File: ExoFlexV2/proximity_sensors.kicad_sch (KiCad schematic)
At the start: 35 parts, among them U31 SN74LVC3G14DCUT_V2, U32 SN74LV4T08PWR_V2, U33 SN74HC7032D_V2, U37 SN74AUP1G17DCKR, U38 SN74AUP1G17DCKR, U39 SN74AUP1G17DCKR, U40 SN74AUP1G17DCKR, U41 SN74AUP1G17DCKR, U8 SN74LV4T08PWR_V2

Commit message: quque truc
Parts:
- removed C92, C93, C94, C95, C96: 0,1uF, Capacitor_SMD:C_0603_1608Metric, symbol Device:C
- removed R47, R48, R49, R50, R51: R_Small_US, Resistor_SMD:R_0603_1608Metric, symbol Device:R_Small_US
- removed TP25, TP27, TP28, TP29: 5005, FootPrint:KEYSTONE_5005, symbol SymLib:5005
- removed U37, U38, U39, U40, U41: SN74AUP1G17DCKR, FootPrint:SN74AUP, symbol SymLib:SN74AUP1G17DCKR
- added R88, R89, R90, R94, R95: 0 ohm, Resistor_SMD:R_0603_1608Metric, symbol Device:R_Small_US
- added TP61, TP62, TP63, TP64, TP65, TP66, TP68, TP69, TP70, TP71, TP72: 5005, FootPrint:KEYSTONE_5005, symbol SymLib:5005
- added U18, U38: 74LV244PW, FootPrint:DB20, symbol SymLib:74LV244PW
- C117: renamed from C87; footprint (none) -> Capacitor_SMD:C_0603_1608Metric
- C118: renamed from C88; footprint (none) -> Capacitor_SMD:C_0603_1608Metric
- C119: renamed from C89; footprint (none) -> Capacitor_SMD:C_0603_1608Metric
- C120: renamed from C90; footprint (none) -> Capacitor_SMD:C_0603_1608Metric
- C121: renamed from C91; footprint (none) -> Capacitor_SMD:C_0603_1608Metric
- renumbered C97 to C122, R42 to R91, R43 to R92, R44 to R93, R45 to R96, R46 to R97, TP26 to TP67, U31 to U33, U32 to U34, U33 to U35, U8 to U9
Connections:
- net +5V: now also U38.20 (VCC)
- net BUT_PROX_1: now also R95.2
- net BUT_PROX_2: now also R94.2
- net BUT_PROX_SEC: now also TP72.TP
- net GND: now also U38.1 (1OE), U38.10 (GND), U38.19 (2OE)
- net PROX_1: now also TP66.TP, U18.5 (2Y1)
- net PROX_2: now also TP67.TP, U18.7 (2Y2)
- net PROX_3: now also TP68.TP, U18.9 (2Y3)
- net PROX_OUT_1: now also R90.2
- net PROX_OUT_2: now also R91.1, R88.2
- net PROX_OUT_3: now also R89.2
- net PROX_SEC: now also TP71.TP
- net at C119.1, R93.2: now also U18.11 (2A3)
- net at C117.1, R91.2: now also U18.13 (2A2)
- net at U9.2 (1B): now also TP70.TP, U38.16 (1Y1)
- net at C120.1, R96.2: now also U38.4 (1A1)
- net at C121.1, R97.2: now also U38.2 (1A0)
- net at C118.1, R92.2: now also U18.15 (2A1)
- net at U9.1 (1A): now also TP69.TP, U38.18 (1Y0)
- new net: R89.1, TP62.TP
- new net: R94.1, TP64.TP
- new net: R90.1, TP63.TP
- new net: R95.1, TP65.TP
- new net: R88.1, TP61.TP
- no-connect marks 5 -> 0
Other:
- moved on the sheet: TP67

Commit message: Placement
Début du placement et modification d'après dernier review
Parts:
- removed R94: 0 ohm, Resistor_SMD:R_0603_1608Metric, symbol Device:R_Small_US
- removed TP64, TP69, TP70: 5005, FootPrint:KEYSTONE_5005, symbol SymLib:5005
- added R84: 0Ω, Resistor_SMD:R_0603_1608Metric, symbol Device:R_Small_US
- added TP107, TP111, TP112, TP113, TP114, TP115: 5005, FootPrint:KEYSTONE_5005, symbol SymLib:5005
- R80: renamed from R90; value 0 ohm -> 0Ω
- R81: renamed from R88; value 0 ohm -> 0Ω
- R82: renamed from R89; value 0 ohm -> 0Ω
- R83: renamed from R95; value 0 ohm -> 0Ω
- renumbered C118 to C121, C117 to C122, C119 to C123, C121 to C124, C120 to C125, C122 to C126, R92 to R85, R91 to R86, R93 to R87, R97 to R88, R96 to R89, TP63 to TP103, TP61 to TP104, TP62 to TP105, TP65 to TP106, TP66 to TP108, TP67 to TP109, TP68 to TP110, TP71 to TP116, TP72 to TP117, U18 to U17, U38 to U18, U9 to U8
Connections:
- net BUT_PROX_2: now also R84.2
- net at U34.11 (4Y), U35.10 (3B): now also TP115.TP
- net at U33.5 (2Y), U34.12 (4A): now also TP113.TP
- net PROX_4: now reaches U18.18 (1Y0), U8.1 (1A)
- net PROX_4: now also TP111.TP
- net PROX_5: now reaches U18.16 (1Y1), U8.2 (1B)
- net PROX_5: now also TP112.TP
- net at U35.6 (2Y), U35.9 (3A): now also TP114.TP
- new net: R84.1, TP107.TP
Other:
- moved on the sheet: C121, C122, C123, C124, C125, R80, R83, R85, R86, R87, R88, R89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

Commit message: Placement encore
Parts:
- removed U17, U18: 74LV244PW, FootPrint:DB20, symbol SymLib:74LV244PW
- added U3: 74LV244PW, FootPrint:DB20, symbol SymLib:74LV244PW
- C122: renamed from C121; value 10 uF -> 10uF
- C123: renamed from C122; value 10 uF -> 10uF
- C124: renamed from C123; value 10 uF -> 10uF
- C125: renamed from C124; value 10 uF -> 10uF
- C126: renamed from C125; value 10 uF -> 10uF
- renumbered C126 to C127, R80 to R81, R81 to R82, R82 to R83, R83 to R84, R84 to R85, R85 to R86, R86 to R87, R87 to R88, R88 to R89, R89 to R90, U8 to U9
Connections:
- net PROX_1: now also U3.3 (2Y0)
- net PROX_2: now also U3.5 (2Y1)
- net PROX_3: now also U3.7 (2Y2)
- net PROX_4: now also U3.14 (1Y2)
- net PROX_5: now also U3.12 (1Y3)
- net at C124.1, R88.2: now also U3.13 (2A2)
- net at C125.1, R89.2: now also U3.6 (1A2)
- net at C123.1, R87.2: now also U3.15 (2A1)
- net at C126.1, R90.2: now also U3.8 (1A3)
- net at C122.1, R86.2: now also U3.17 (2A0)

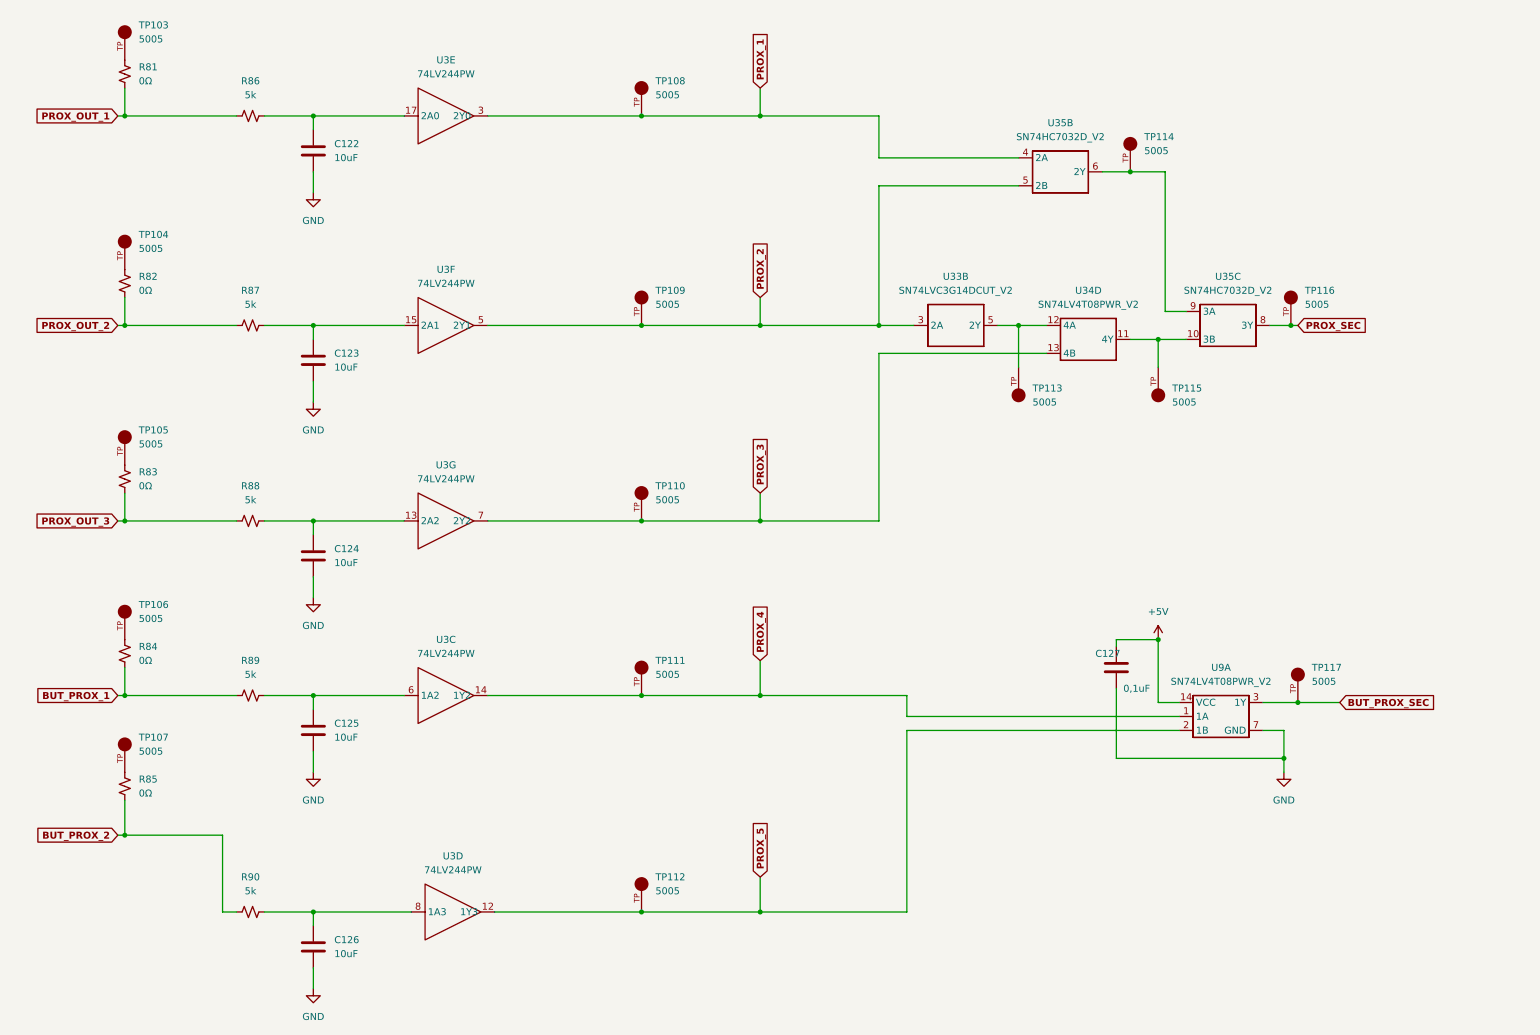
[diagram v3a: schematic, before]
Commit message: Mise à jour mi-stage
- Torque et Amplitude testé et vérifié
- Capteur de présence et de proximité testé
- Système de détection de coupure de fils
- Polyvalence pour plusieurs capteurs
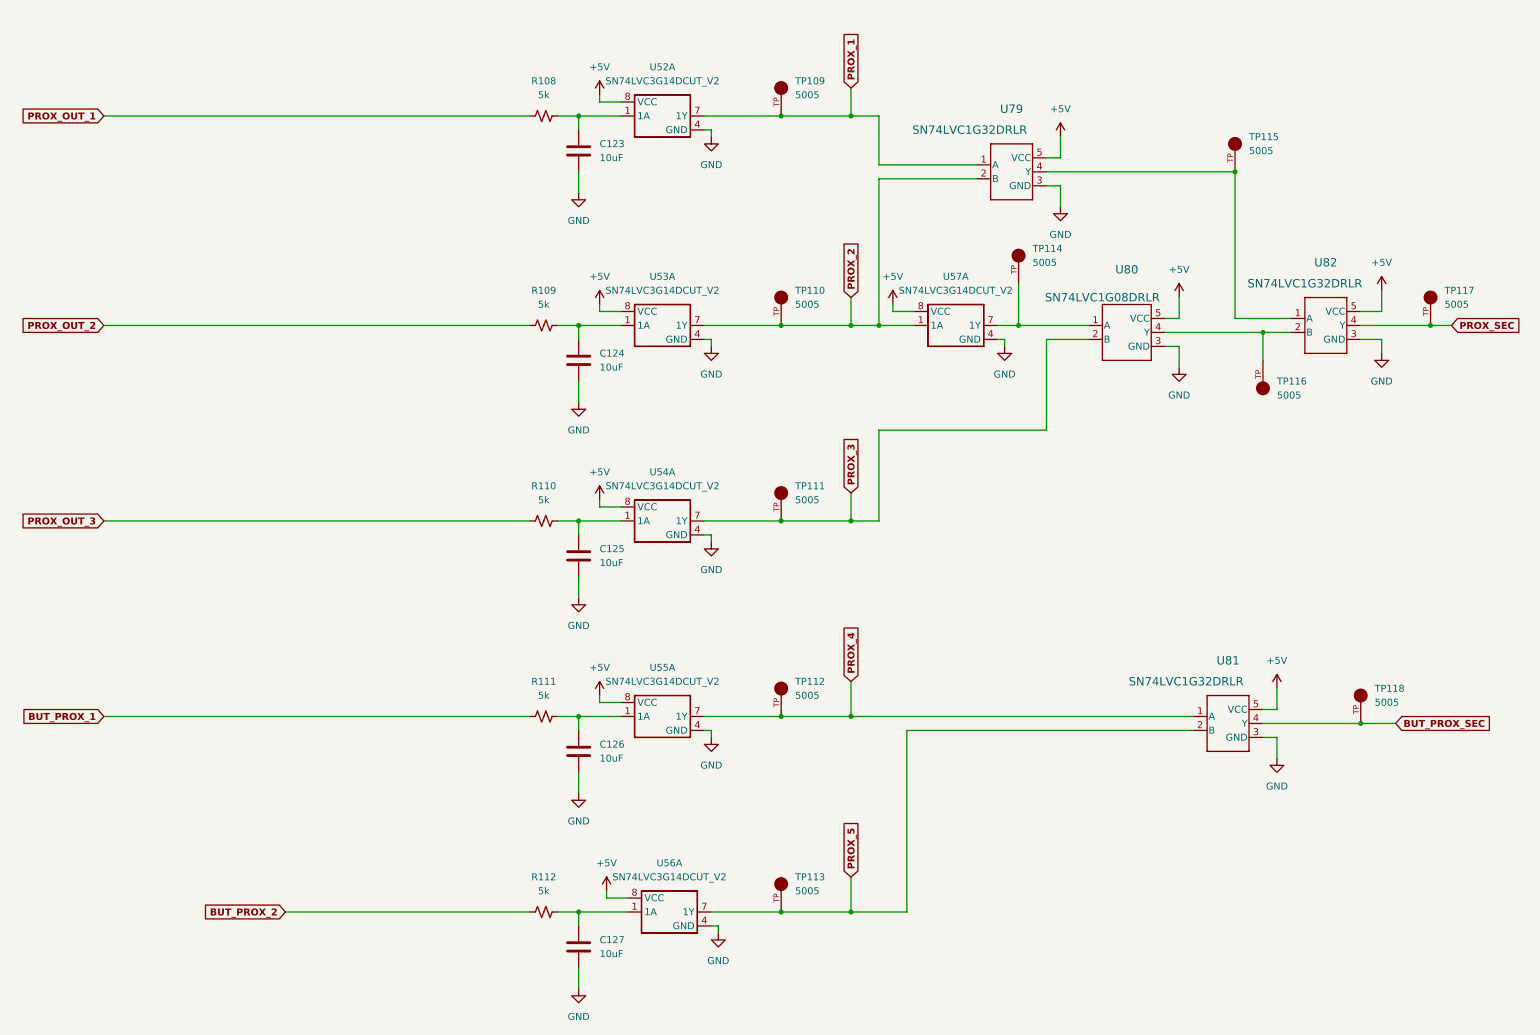
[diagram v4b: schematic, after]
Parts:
- removed C127: 0,1uF, Capacitor_SMD:C_0603_1608Metric, symbol Device:C
- removed R81, R82, R83, R84, R85: 0Ω, Resistor_SMD:R_0603_1608Metric, symbol Device:R_Small_US
- removed TP103, TP104, TP105, TP106, TP107: 5005, FootPrint:KEYSTONE_5005, symbol SymLib:5005
- removed U3: 74LV244PW, FootPrint:DB20, symbol SymLib:74LV244PW
- removed U33: SN74LVC3G14DCUT_V2, FootPrint:SN74LVC3G14DCUT, symbol SymLib:SN74LVC3G14DCUT_V2
- removed U34, U9: SN74LV4T08PWR_V2, FootPrint:SN74LV4T08PWR, symbol SymLib:SN74LV4T08PWR_V2
- removed U35: SN74HC7032D_V2, FootPrint:SN74HC7032D, symbol SymLib:SN74HC7032D_V2
- added U52, U53, U54, U55, U56, U57: SN74LVC3G14DCUT_V2, FootPrint:SN74LVC3G14DCUT, symbol SymLib:SN74LVC3G14DCUT_V2
- added U79, U81, U82: SN74LVC1G32DRLR, FootPrint:DRL5, symbol SymLib:SN74LVC1G32DRLR
- added U80: SN74LVC1G08DRLR, FootPrint:DRL5, symbol SymLib:SN74LVC1G08DRLR
- renumbered C122 to C123, C123 to C124, C124 to C125, C125 to C126, C126 to C127, R86 to R108, R87 to R109, R88 to R110, R89 to R111, R90 to R112, TP108 to TP109, TP109 to TP110, TP110 to TP111, TP111 to TP112, TP112 to TP113, TP113 to TP114, TP114 to TP115, TP115 to TP116, TP116 to TP117, TP117 to TP118
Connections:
- net +5V: now also U52.8 (VCC), U53.8 (VCC), U54.8 (VCC), U55.8 (VCC), U56.8 (VCC), U57.8 (VCC), U79.5 (VCC), U80.5 (VCC), U81.5 (VCC), U82.5 (VCC)
- net BUT_PROX_SEC: now also U81.4 (Y)
- net GND: now also U52.4 (GND), U53.4 (GND), U54.4 (GND), U55.4 (GND), U56.4 (GND), U57.4 (GND), U79.3 (GND), U80.3 (GND), U81.3 (GND), U82.3 (GND)
- net PROX_1: now also U52.7 (1Y), U79.1 (A)
- net PROX_2: now also U53.7 (1Y), U57.1 (1A), U79.2 (B)
- net PROX_3: now also U54.7 (1Y), U80.2 (B)
- net PROX_4: now also U55.7 (1Y), U81.1 (A)
- net PROX_5: now also U56.7 (1Y), U81.2 (B)
- net PROX_SEC: now also U82.4 (Y)
- net at TP116.TP: now also U80.4 (Y), U82.2 (B)
- net at TP114.TP: now also U57.7 (1Y), U80.1 (A)
- net at C125.1, R110.2: now also U54.1 (1A)
- net at C127.1, R112.2: now also U56.1 (1A)
- net at C124.1, R109.2: now also U53.1 (1A)
- net at C126.1, R111.2: now also U55.1 (1A)
- net at TP115.TP: now also U79.4 (Y), U82.1 (A)
- net at C123.1, R108.2: now also U52.1 (1A)
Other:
- moved on the sheet: C123, C124, C125, C126, C127, R108, R109, R110, R111, R112, TP109, TP110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
